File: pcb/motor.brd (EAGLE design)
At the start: 44.4 x 77.8 mm, 25 parts, among them X1 MST2V, X2 MST4V, X3 MST2V, X4 MST2V

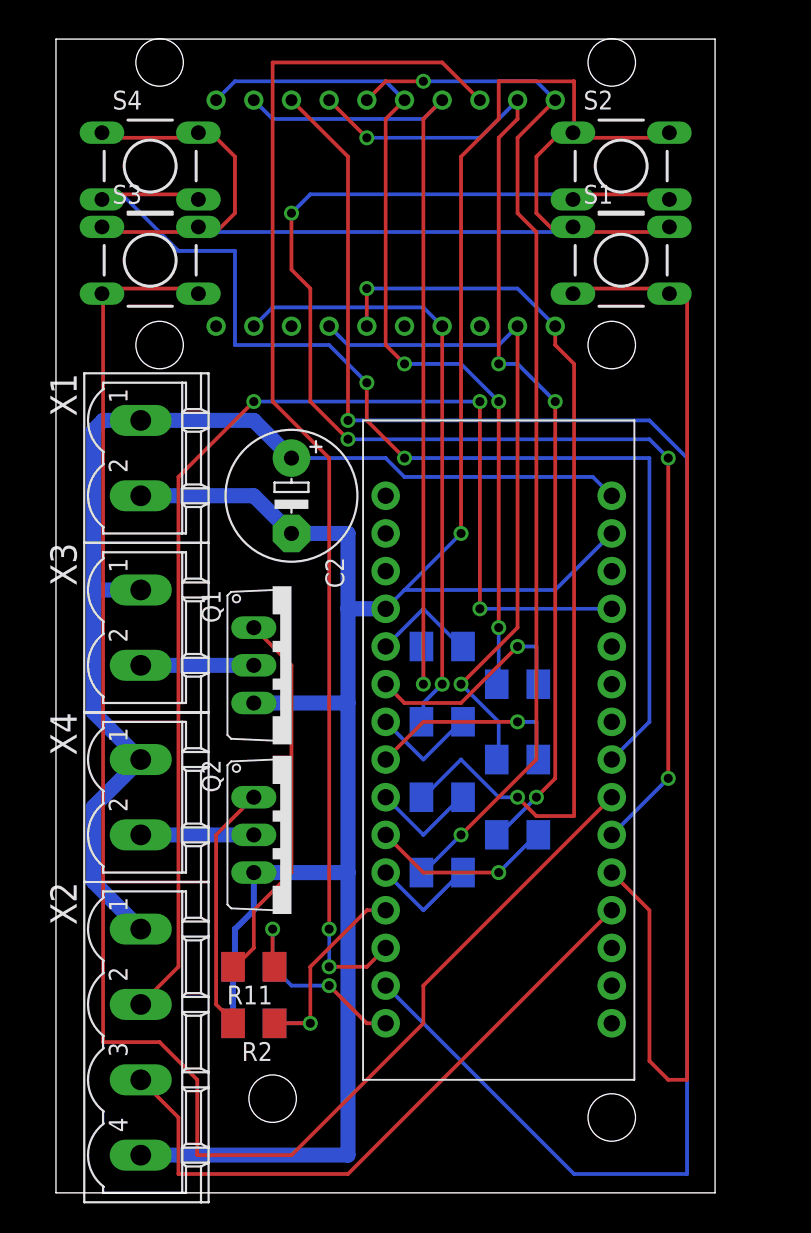
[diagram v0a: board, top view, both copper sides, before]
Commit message: updated schematic for motor driver
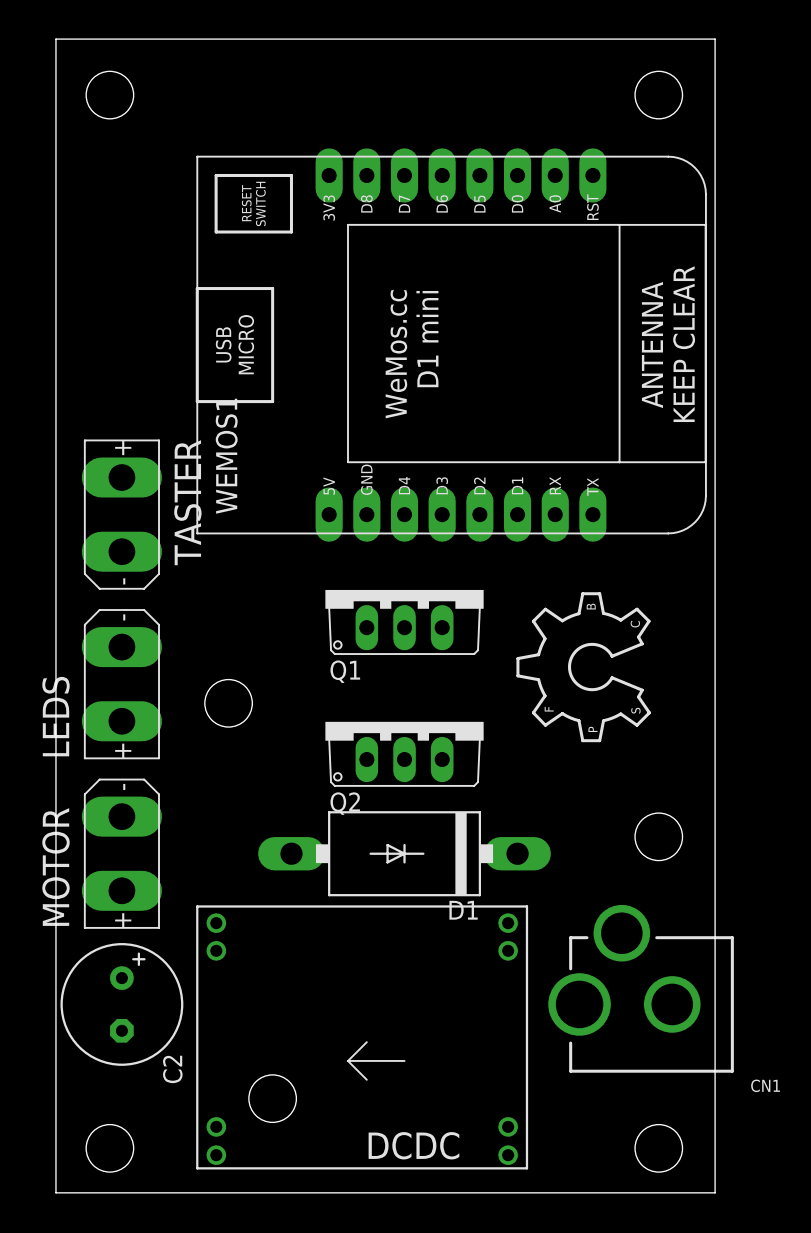
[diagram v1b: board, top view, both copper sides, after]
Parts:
- removed LED1, LED2: 7-SEG_SA52-11, display-kingbright:SA52-11
- removed R1, R3: 100K, rcl:M1206
- removed R10, R4, R5, R6, R7, R8, R9: 1K, rcl:M1206
- removed R11, R2: 10R, rcl:M1206
- removed S1, S2, S3, S4: DTS-6, switch-tact:DTS-6
- removed U$2: ARDUINOMICRO_NEW, adafruit:ARDUINOMIRCO_NEW
- removed X1, X3, X4: MST2V, con-phoenix-508:MSTBV2
- removed X2: MST4V, con-phoenix-508:MSTBV4
- added CN1: (no value), microbuilder:DCJACK_2MM_PTH
- added D1: 1N5400, diode:DO201-15
- added DCDC: DCDC, main:DCDC
- added LEDS, MOTOR, TASTER: TX30, main:XT30
- added LOGO1: OSHW_LOGO_FILLX0350-NT, ohw-logo:OSHW_FILLX350_NOTEXT
- added WEMOS1: (no value), esp8266modules:WEMOS-D1-MINI
- C2: device rcl:E5-8,5 -> rcl:E3,5-8
- Q1, Q2: value (none) -> IRF3708
- moved C2 36.1 mm to (3.81, 12.7)
- moved Q2 10.8 mm to (22.9, 31.8), turned to 0 degrees
- moved Q1 9.16 mm to (22.9, 40.6), turned to 0 degrees
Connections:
- removed net N$10: R5.2, U$2.P$10
- removed net N$11: LED1.9, LED2.9, R9.1
- removed net N$12: R7.2, U$2.P$9
- removed net N$13: R6.2, U$2.P$8
- removed net N$14: R8.2, U$2.P$7
- removed net N$15: R9.2, U$2.P$6
- removed net N$16: R10.2, U$2.P$5
- removed net N$17: U$2.P$34
- removed net N$18: U$2.P$23, X2.2
- removed net N$19: S3.3, S3.4, U$2.P$28
- removed net N$20: R11.1, R3.1, U$2.P$1
- removed net N$21: S2.3, S2.4, U$2.P$29
- removed net N$22: S1.3, S1.4, U$2.P$30
- removed net N$30: LED1.1, LED2.1, R8.1
- removed net N$31: LED1.2, LED2.2, R6.1
- removed net N$32: LED1.4, LED2.4, R7.1
- removed net N$33: LED1.6, LED2.6, R5.1
- removed net N$34: LED1.7, LED2.7, R4.1
- removed net N$35: LED1.8, U$2.P$3
- removed net N$36: LED2.8, U$2.P$2
- removed net N$6: Q2.1, R2.2
- removed net N$7: U$2.P$31, X2.3
- removed net N$8: R4.2, U$2.P$11
- removed net N$9: LED1.10, LED2.10, R10.1
- new net +5V: C2.+, DCDC.VOUT1, DCDC.VOUT2, WEMOS1.5V
- net +12V: now also CN1.PWR, D1.C, DCDC.VIN1, DCDC.VIN2, LEDS.P, MOTOR.P; no longer C2.+, U$2.P$20, X1.1, X2.1, X3.1, X4.1
- net GND: now also CN1.GND, CN1.GNDBREAK, DCDC.GND1, DCDC.GND2, DCDC.GND3, DCDC.GND4, TASTER.N, WEMOS1.GND; no longer R1.2, R3.2, S1.1, S1.2, S2.1, S2.2, S3.1, S3.2, S4.1, S4.2, U$2.P$12, U$2.P$21, X1.2, X2.4
- net N$1: now also D1.A, MOTOR.N; no longer X4.2
- net N$2: now also LEDS.N; no longer X3.2
- net N$3: now also WEMOS1.D1; no longer R11.2
- net N$4: now also TASTER.P, WEMOS1.D5; no longer S4.3, S4.4, U$2.P$27
- net N$5: now also Q2.1, WEMOS1.D2; no longer R1.1, R2.1, U$2.P$4
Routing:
- net GND: track 233.4 -> 0.00 mm, vias 1 -> 0
- net N$36: track 120.9 -> 0.00 mm, vias 1 -> 0
- net N$19: track 109.8 -> 0.00 mm
- net N$21: track 92.5 -> 0.00 mm, vias 4 -> 0
- net N$35: track 81.9 -> 0.00 mm, vias 2 -> 0
- net N$18: track 81.9 -> 0.00 mm, vias 3 -> 0
- net N$22: track 78.5 -> 0.00 mm
- net N$4: track 78.2 -> 0.00 mm, vias 2 -> 0
- net +12V: track 78.1 -> 0.00 mm
- net N$9: track 70.7 -> 0.00 mm, vias 2 -> 0
- net N$11: track 68.9 -> 0.00 mm, vias 4 -> 0
- net N$30: track 62.8 -> 0.00 mm, vias 2 -> 0
- net N$33: track 59.2 -> 0.00 mm, vias 3 -> 0
- net N$34: track 56.3 -> 0.00 mm, vias 1 -> 0
- net N$31: track 45.7 -> 0.00 mm, vias 1 -> 0
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
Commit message: first version of motor driver pcb layout
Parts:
- removed DCDC: DCDC, main:DCDC
- added R1, R2: 180R, rcl:0207/10
- added U$1: LOGO20MM, im-pro-logo:LOGO_20MM
- added U$2: DCDC_5V, diypov:DCDC
- C2: value (none) -> 100u
- moved LOGO1 41.3 mm to (9.53, 59.1)
- moved Q1 8.08 mm to (17.1, 34.9), turned to 90 degrees
- moved Q2 6.54 mm to (28.6, 34.9), turned to 90 degrees
- moved TASTER 5.75 mm to (3.17, 51.4), turned to 90 degrees
- moved LEDS 4.49 mm to (3.17, 38.7)
- moved WEMOS1 3.86 mm to (24.1, 59.1), turned to 180 degrees
- moved D1 3.24 mm to (19.7, 23.5), turned to 0 degrees
- moved MOTOR 3.24 mm to (3.17, 26.0)
- moved C2 0.90 mm to (4.45, 13.3)
- moved CN1 0.90 mm to (47.6, 13.3)
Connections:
- new net N$6: Q2.1, R2.2
- new net N$7: Q1.1, R1.2
- net +12V: now also U$2.VIN1, U$2.VIN2; no longer DCDC.VIN1, DCDC.VIN2
- net +5V: now also U$2.VOUT1, U$2.VOUT2; no longer DCDC.VOUT1, DCDC.VOUT2
- net GND: now also U$2.GND1, U$2.GND2, U$2.GND3, U$2.GND4; no longer DCDC.GND1, DCDC.GND2, DCDC.GND3, DCDC.GND4
- net N$3: now also R1.1; no longer Q1.1
- net N$5: now also R2.1; no longer Q2.1
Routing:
- net +5V: track 0.00 -> 120.9 mm
- net N$4: track 0.00 -> 57.8 mm
- net +12V: track 0.00 -> 53.0 mm
- net N$1: track 0.00 -> 41.2 mm
- net N$5: track 0.00 -> 32.7 mm
- net N$3: track 0.00 -> 24.6 mm
- net N$2: track 0.00 -> 24.5 mm
- net N$7: track 0.00 -> 7.62 mm
- net N$6: track 0.00 -> 7.62 mm
- added copper zone on layer 1, net GND
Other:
- board size 44.4 x 77.8 mm -> 44.4 x 78.4 mm
- board text added: "DIY POV Display Motor Driver"

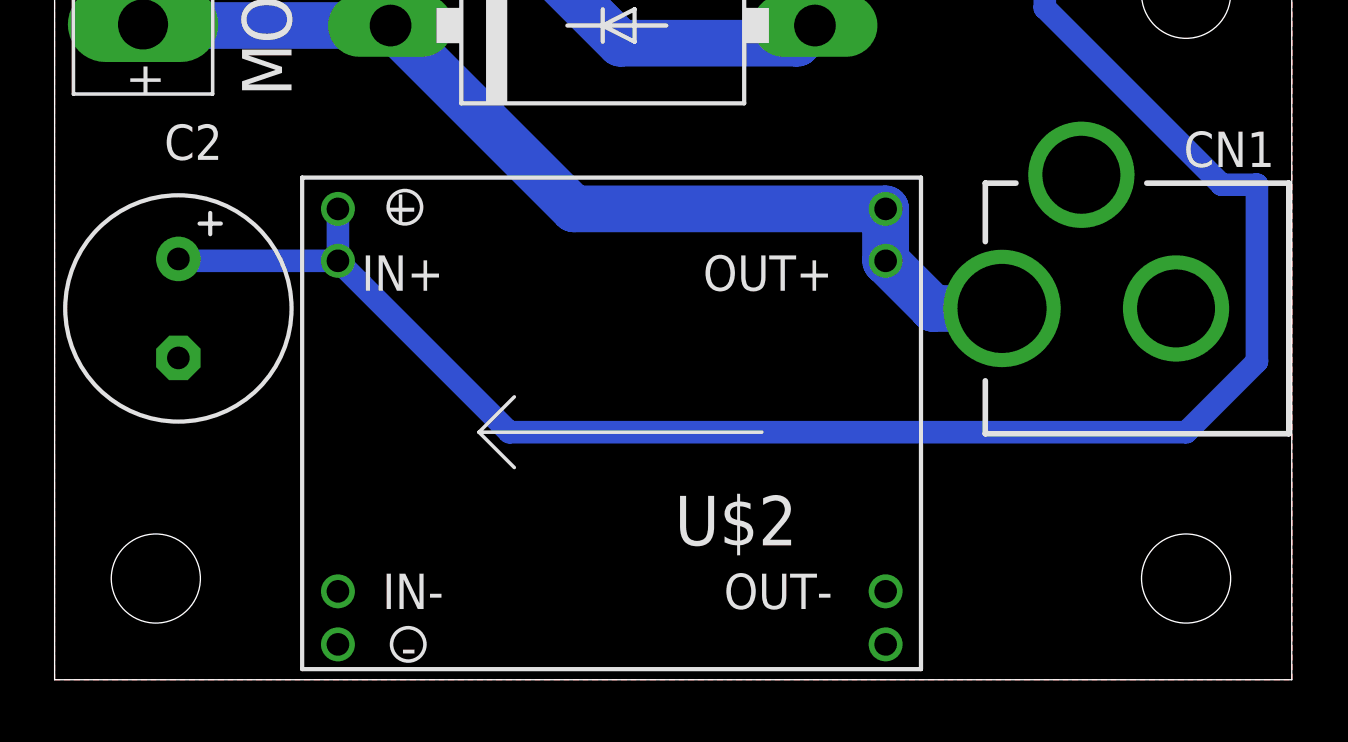
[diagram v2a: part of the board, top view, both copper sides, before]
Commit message: finished main pcb layout
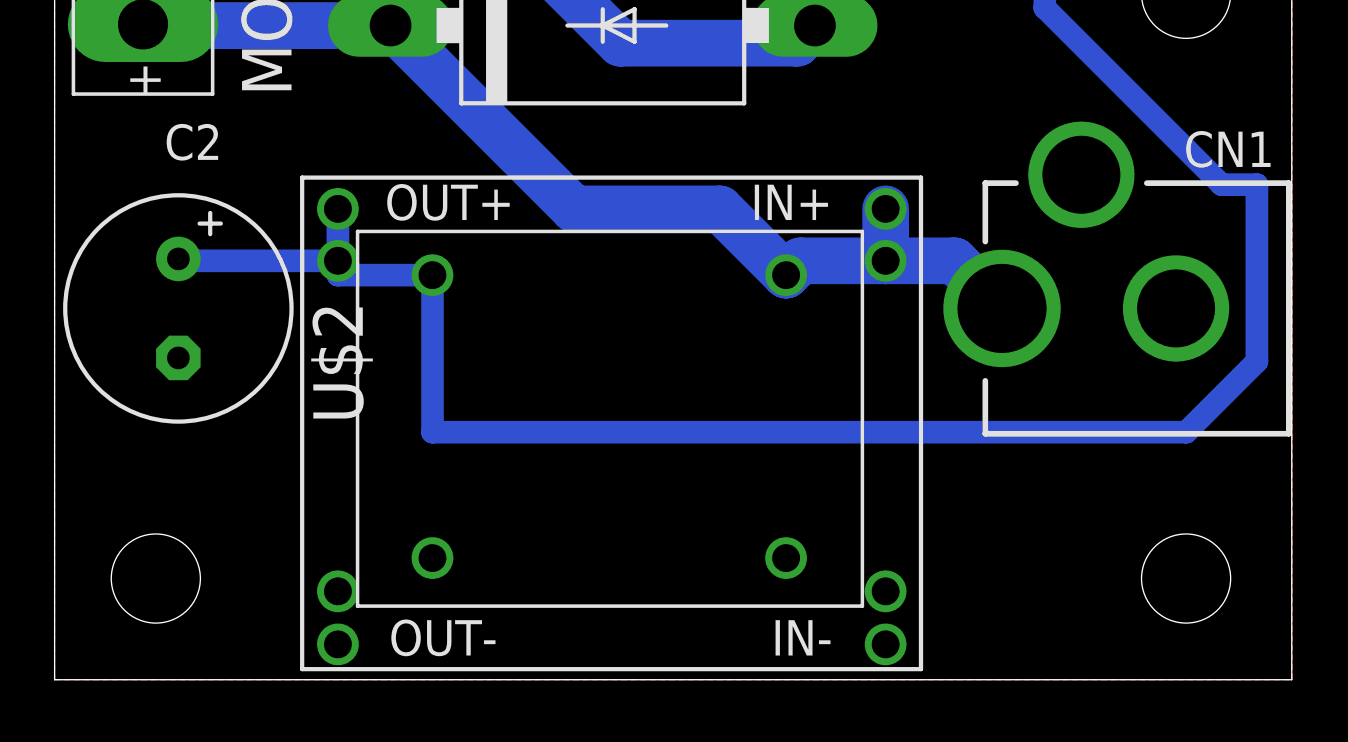
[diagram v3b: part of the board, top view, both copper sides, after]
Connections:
- net +12V: now also U$2.VIN3
- net +5V: now also U$2.VOUT3
- net GND: now also U$2.GND5, U$2.GND6
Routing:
- net +5V: track 120.9 -> 124.7 mm
- net +12V: track 53.0 -> 54.2 mm

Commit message: layout finished
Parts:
- C2: value 100u -> 220u
- renumbered U$2 to DCDC
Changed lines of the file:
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@@
 <layer number="49" name="Reference" color="7" fill="1" visible="yes" active="yes"/>
 <layer number="50" name="dxf" color="7" fill="1" visible="no" active="no"/>
-<layer number="51" name="tDocu" color="7" fill="1" visible="yes" active="yes"/>
-<layer number="52" name="bDocu" color="7" fill="1" visible="yes" active="yes"/>
+<layer number="51" name="tDocu" color="7" fill="1" visible="no" active="yes"/>
+<layer number="52" name="bDocu" color="7" fill="1" visible="no" active="yes"/>
 <layer number="53" name="tGND_GNDA" color="7" fill="9" visible="no" active="no"/>
 <layer number="54" name="bGND_GNDA" color="1" fill="9" visible="no" active="no"/>
@@
 <attribute name="NAME" x="8.509" y="46.355" size="1.778" layer="25" ratio="10" rot="R90"/>
 </element>
-<element name="C2" library="rcl" package="E3,5-8" value="100u" x="4.445" y="13.335" smashed="yes" rot="R270">
+<element name="C2" library="rcl" package="E3,5-8" value="220u" x="4.445" y="13.335" smashed="yes" rot="R270">
 <attribute name="NAME" x="3.937" y="18.669" size="1.27" layer="25" ratio="10"/>
 <attribute name="VALUE" x="1.397" y="15.621" size="1.27" layer="27" ratio="10" rot="R270"/>
 </element>
 <element name="CN1" library="microbuilder" package="DCJACK_2MM_PTH" value="" x="47.625" y="13.335" smashed="yes" rot="R90">
-<attribute name="NAME" x="43.815" y="19.685" size="1.27" layer="25" ratio="18" rot="R180"/>
+<attribute name="NAME" x="43.815" y="17.145" size="1.27" layer="25" ratio="18" rot="R180"/>
 <attribute name="VALUE" x="47.625" y="18.669" size="0.4064" layer="27" ratio="10" rot="R180"/>
 </element>
 <element name="LEDS" library="main" package="XT30" value="TX30" x="3.175" y="38.735" smashed="yes" rot="R90">
-<attribute name="NAME" x="8.509" y="33.655" size="1.778" layer="25" ratio="10" rot="R90"/>
+<attribute name="NAME" x="8.509" y="34.925" size="1.778" layer="25" ratio="10" rot="R90"/>
 </element>
 <element name="MOTOR" library="main" package="XT30" value="TX30" x="3.175" y="26.035" smashed="yes" rot="R90">
@@
 </element>
 <element name="U$1" library="im-pro-logo" package="LOGO_20MM" value="LOGO20MM" x="43.815" y="49.53" rot="R90"/>
-<element name="U$2" library="diypov" package="DCDC" value="DCDC_5V" x="30.48" y="1.27" rot="R180"/>
+<element name="DCDC" library="diypov" package="DCDC" value="DCDC_5V" x="30.48" y="1.27" rot="R180"/>
 </elements>
 <signals>
@@
 <vertex x="0" y="78.105"/>
 </polygon>
-<contactref element="U$2" pad="GND5"/>
-<contactref element="U$2" pad="GND2"/>
-<contactref element="U$2" pad="GND1"/>
-<contactref element="U$2" pad="GND3"/>
-<contactref element="U$2" pad="GND6"/>
-<contactref element="U$2" pad="GND4"/>
-<contactref element="U$2" pad="GND5"/>
-<contactref element="U$2" pad="GND2"/>
-<contactref element="U$2" pad="GND1"/>
-<contactref element="U$2" pad="GND3"/>
-<contactref element="U$2" pad="GND6"/>
-<contactref element="U$2" pad="GND4"/>
+<contactref element="DCDC" pad="GND5"/>
+<contactref element="DCDC" pad="GND2"/>
+<contactref element="DCDC" pad="GND1"/>
+<contactref element="DCDC" pad="GND3"/>
+<contactref element="DCDC" pad="GND6"/>
+<contactref element="DCDC" pad="GND4"/>
+<contactref element="DCDC" pad="GND5"/>
+<contactref element="DCDC" pad="GND2"/>
+<contactref element="DCDC" pad="GND1"/>
+<contactref element="DCDC" pad="GND3"/>
+<contactref element="DCDC" pad="GND6"/>
+<contactref element="DCDC" pad="GND4"/>
 </signal>
 <signal name="+12V">
@@
 <wire x1="11.43" y1="27.94" x2="11.43" y2="23.495" width="1.6764" layer="1"/>
 <wire x1="11.43" y1="23.495" x2="12.065" y2="23.495" width="1.6764" layer="1"/>
-<contactref element="U$2" pad="VIN3"/>
-<contactref element="U$2" pad="VIN1"/>
-<contactref element="U$2" pad="VIN2"/>
+<contactref element="DCDC" pad="VIN3"/>
+<contactref element="DCDC" pad="VIN1"/>
+<contactref element="DCDC" pad="VIN2"/>
 <wire x1="18.65" y1="16.91" x2="23.89" y2="16.91" width="1.6764" layer="16"/>
 <wire x1="23.89" y1="16.91" x2="26.27" y2="14.53" width="1.6764" layer="16"/>
@@
 <wire x1="43.18" y1="17.78" x2="41.91" y2="17.78" width="0.8128" layer="16"/>
 <wire x1="41.91" y1="17.78" x2="35.56" y2="24.13" width="0.8128" layer="16"/>
-<contactref element="U$2" pad="VOUT2"/>
-<contactref element="U$2" pad="VOUT1"/>
-<contactref element="U$2" pad="VOUT3"/>
+<contactref element="DCDC" pad="VOUT2"/>
+<contactref element="DCDC" pad="VOUT1"/>
+<contactref element="DCDC" pad="VOUT3"/>
 <wire x1="13.57" y1="8.89" x2="13.57" y2="14.53" width="0.8128" layer="16"/>
 <wire x1="13.57" y1="14.53" x2="10.175" y2="14.53" width="0.8128" layer="16"/>
